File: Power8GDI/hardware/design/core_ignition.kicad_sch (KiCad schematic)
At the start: 36 parts, among them U110 MIC4427YM, U111 MIC4427YM, U112 MIC4427YM, U113 MIC4427YM

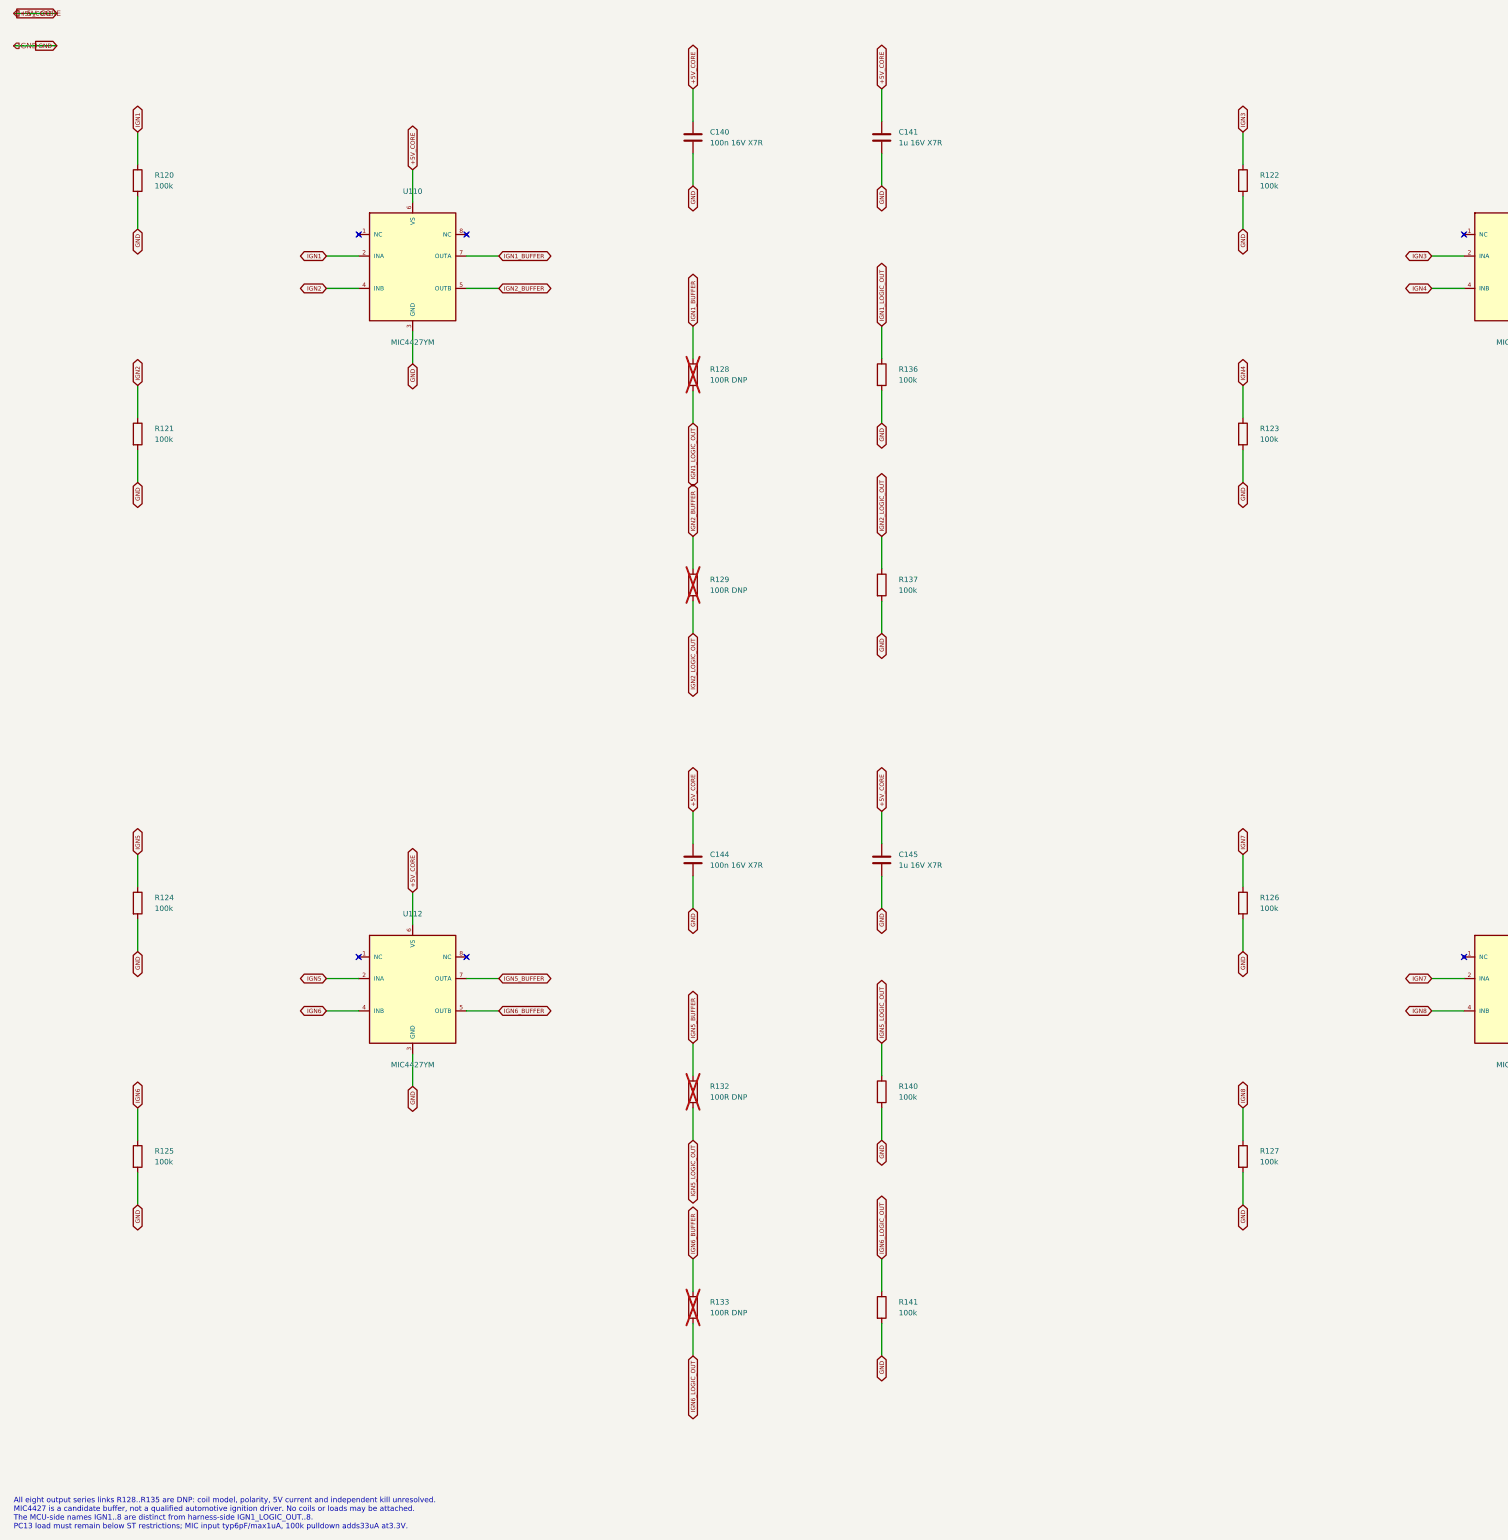
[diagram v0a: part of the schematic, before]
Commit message: Integrate connected ECU schematic and auditable review PCB
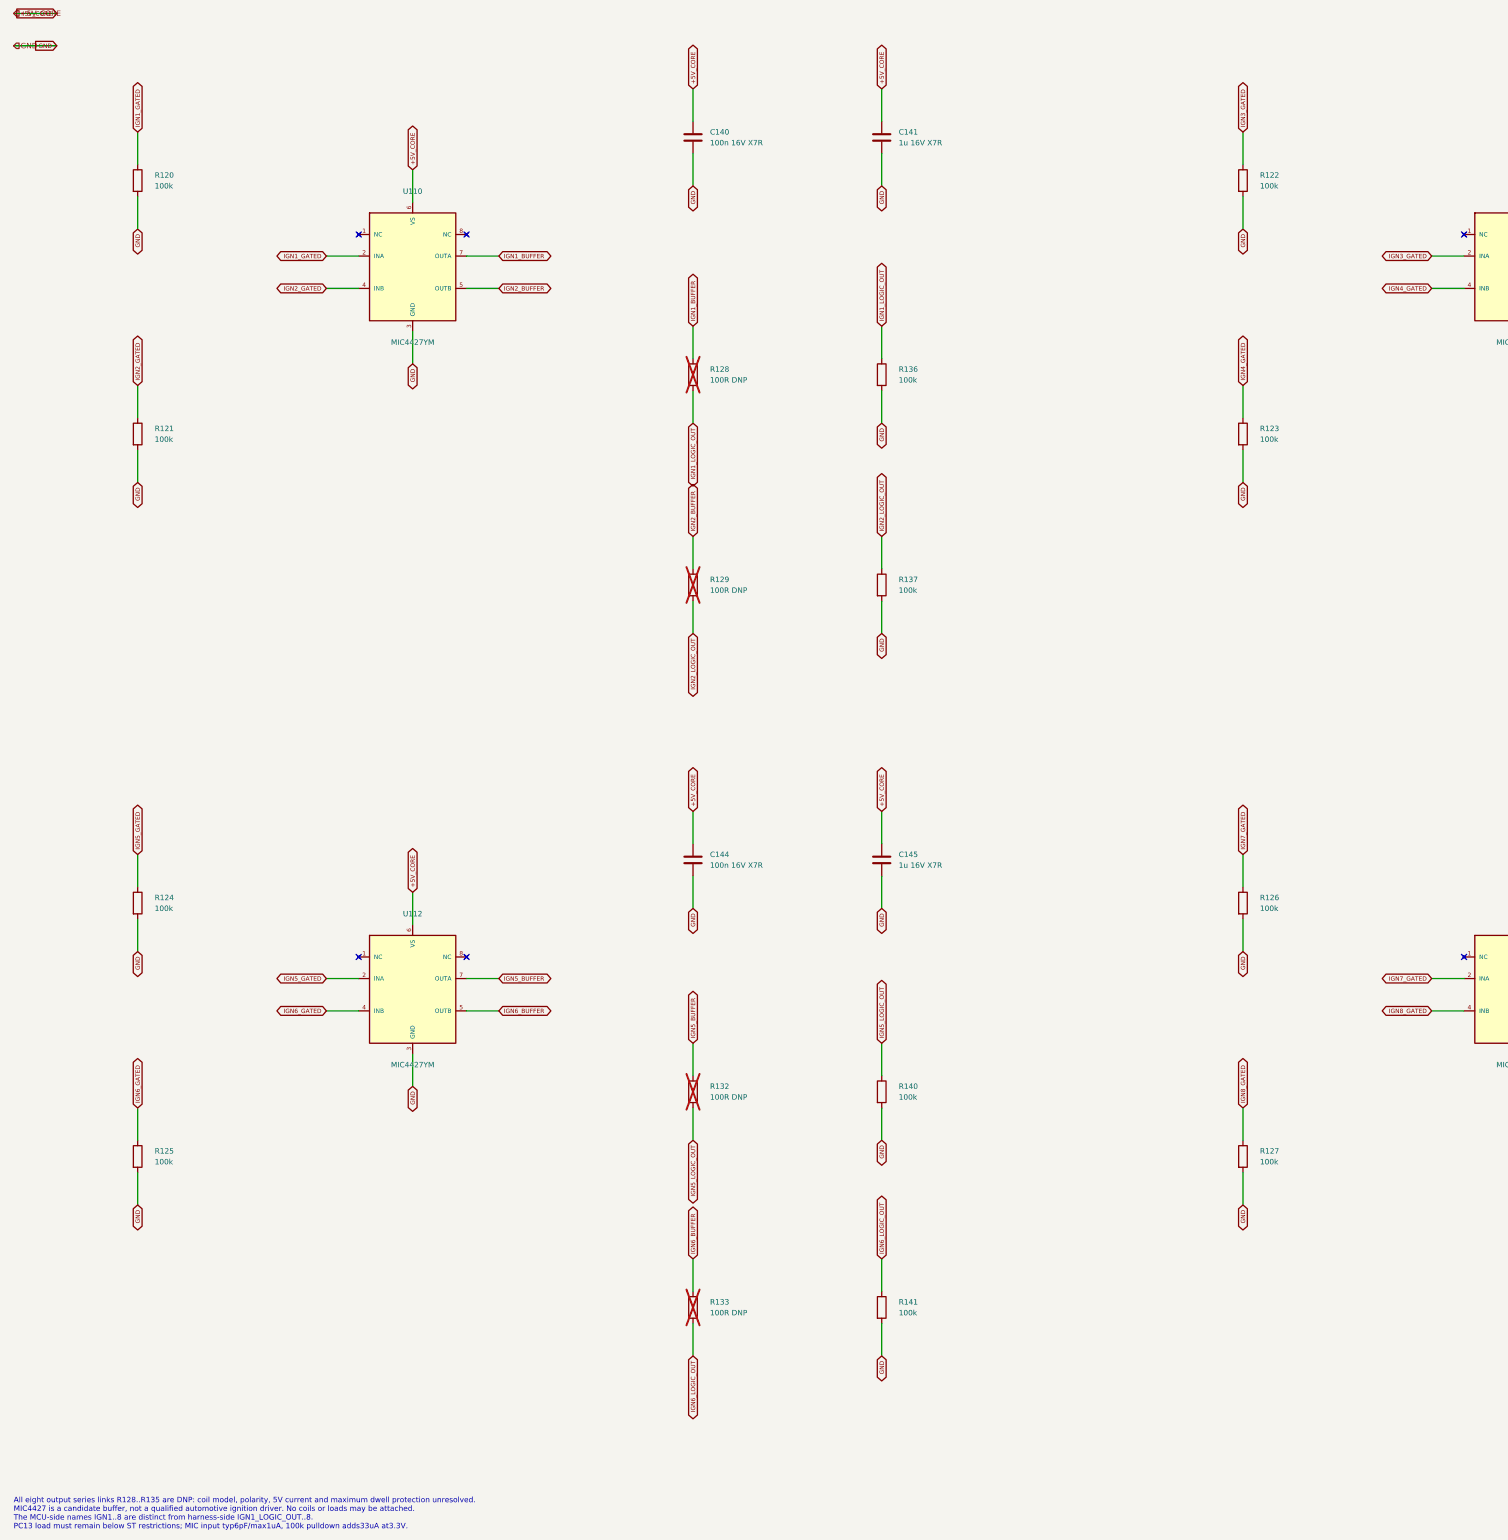
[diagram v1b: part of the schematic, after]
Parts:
- R120, R121, R122, R123, R124, R125, R126, R127: Design note Input defaultlow; PC13 load check includes inputI/C andtrace -> Buffer input default low after hardware permission gate
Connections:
- net IGN1 renamed IGN1_GATED
- net IGN2 renamed IGN2_GATED
- net IGN3 renamed IGN3_GATED
- net IGN4 renamed IGN4_GATED
- net IGN5 renamed IGN5_GATED
- net IGN6 renamed IGN6_GATED
- net IGN7 renamed IGN7_GATED
- net IGN8 renamed IGN8_GATED
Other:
- note added: "All eight output series links R128..R135 are DNP: coil model, polarity, 5V current and maximum dwell protection unresolved. MIC4427 is a candidate buffer, not a qualified automotive ignition driver. No coils or loads may be attached. The MCU-side names IGN1..8 are distinct from harness-side IGN1_LOGIC_OUT..8. PC13 load must remain below ST restrictions; MIC input typ6pF/max1uA, 100k pulldown adds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"
- note removed: "All eight output series links R128..R135 are DNP: coil model, polarity, 5V current and independent kill unresolved. MIC4427 is a candidate buffer, not a qualified automotive ignition driver. No coils or loads may be attached. The MCU-side names IGN1..8 are distinct from harness-side IGN1_LOGIC_OUT..8. PC13 load must remain below ST restrictions; MIC input typ6pF/max1uA, 100k pulldown adds33uA at3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"
